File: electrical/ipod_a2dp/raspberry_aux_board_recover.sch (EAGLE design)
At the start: 23 parts, among them IC1 74LS244N

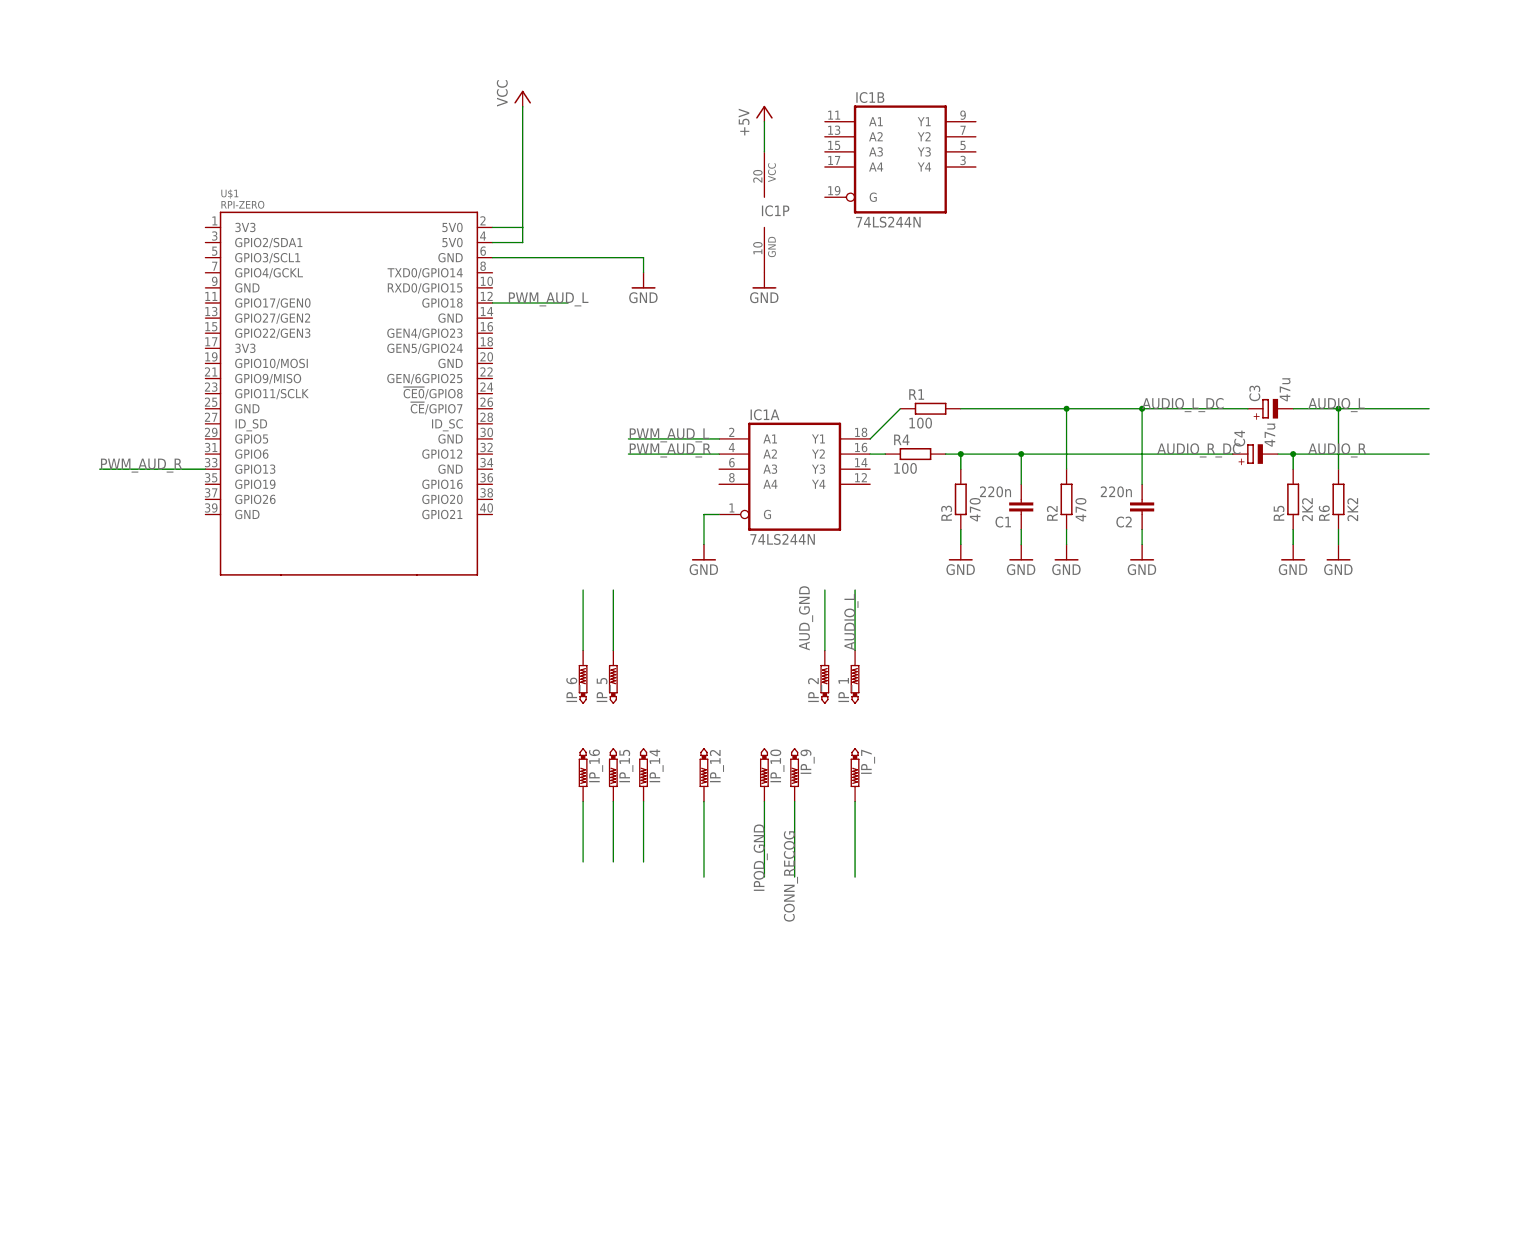
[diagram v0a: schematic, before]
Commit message: more changes. proto tested. working for audio.
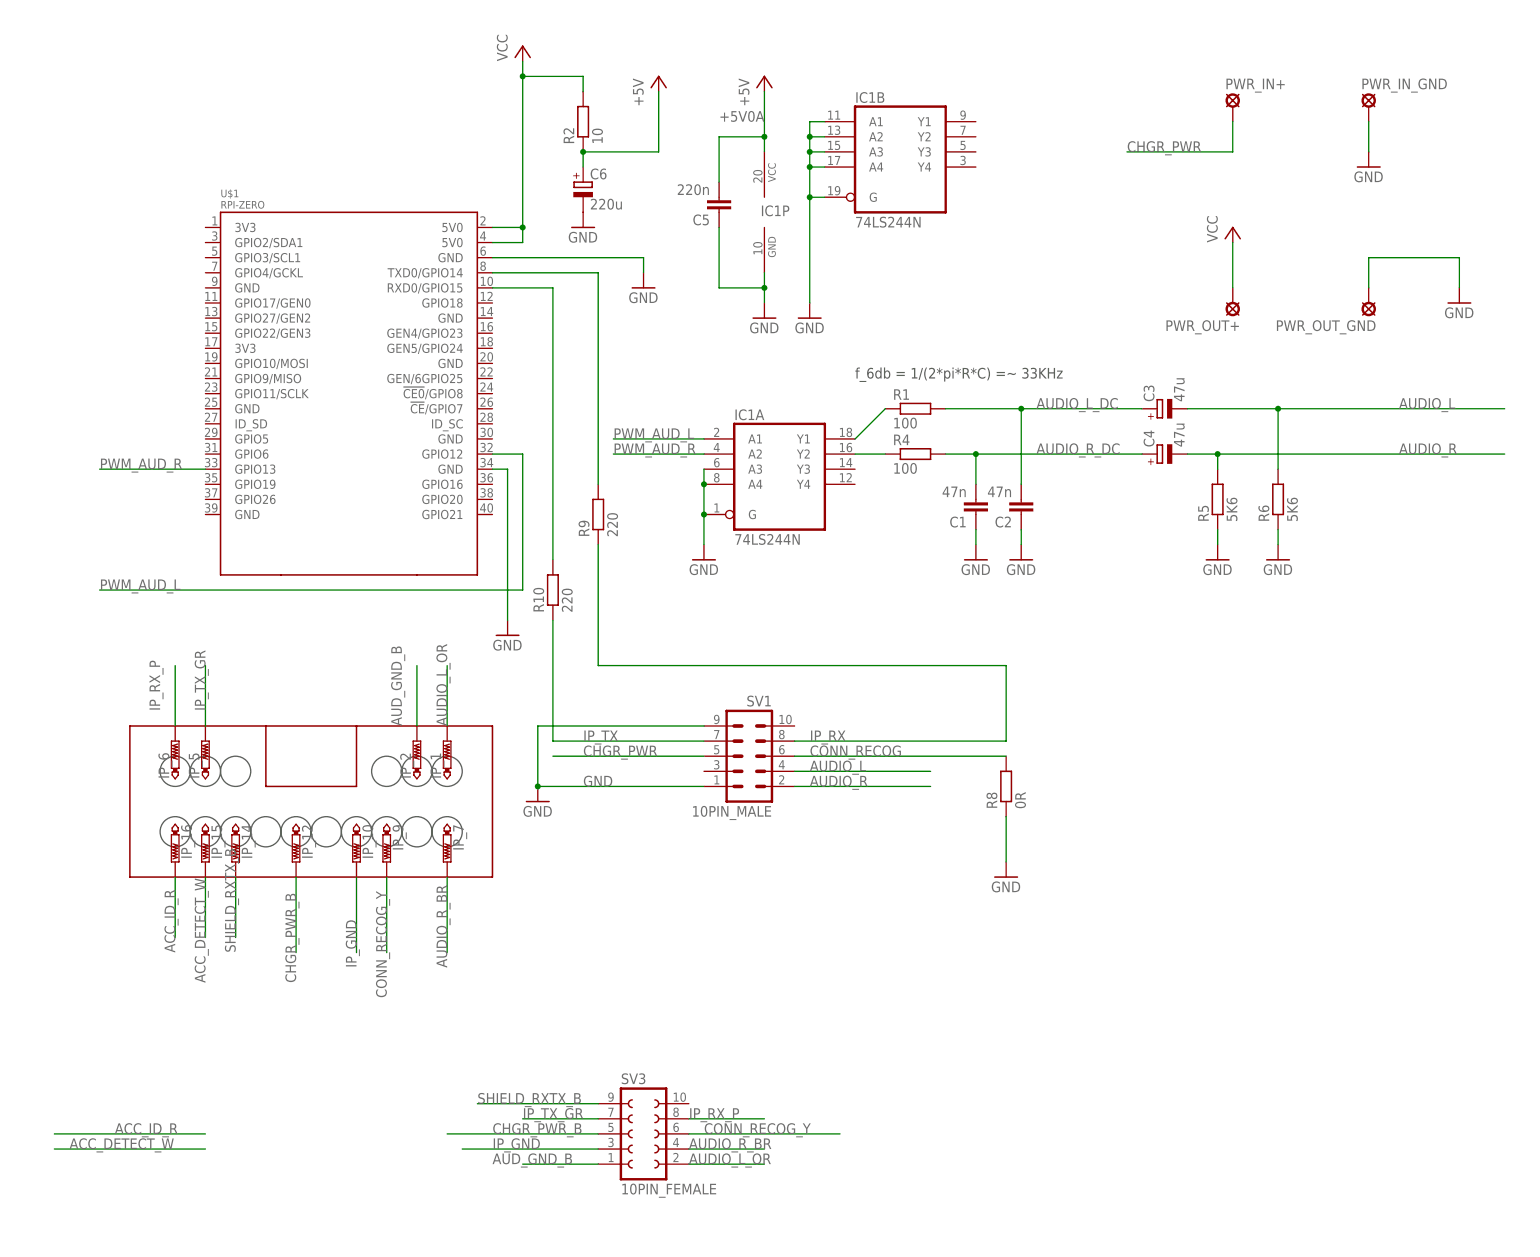
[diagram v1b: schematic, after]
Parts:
- removed R3: 470, rcl:R-EU_0207/10
- added C5: 220n, rcl:C-EU025_050-035X075
- added C6: 220u, rcl:CPOL-EUE2.5-5
- added PWR_IN+, PWR_IN_GND, PWR_OUT+, PWR_OUT_GND: SE13, solpad:SE13
- added R10, R9: 220, rcl:R-EU_0207/10
- added R8: 0R, rcl:R-EU_0207/10
- added SV1: 10PIN_MALE, con-lstb:MA05-2
- added SV3: 10PIN_FEMALE, con-lsta:FE05-2
- C1, C2: value 220n -> 47n
- R2: value 470 -> 10
- R5, R6: value 2K2 -> 5K6
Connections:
- net N$2 renamed ACC_ID_R
- net N$4 renamed ACC_DETECT_W
- removed net +5V: IC1P.VCC
- removed net AUD_GND: IP_2.TP
- removed net IPOD_GND: IP_10.TP
- removed net N$5: IP_5.TP
- removed net N$6: IP_6.TP
- removed net N$7: IP_14.TP
- removed net N$8: IP_12.TP
- new net +5V0A: C5.2, C6.+, IC1P.VCC, R2.1
- new net AUDIO_L_OR: IP_1.TP, SV3.2
- new net AUDIO_R_BR: IP_7.TP, SV3.4
- new net AUD_GND_B: IP_2.TP, SV3.1
- new net CHGR_PWR: PWR_IN+.MP, SV1.5
- new net CHGR_PWR_B: IP_12.TP, SV3.5
- new net CONN_RECOG_Y: IP_9.TP, SV3.6
- new net IP_GND: IP_10.TP, SV3.3
- new net IP_RX: R9.1, SV1.8
- new net IP_RX_P: IP_6.TP, SV3.8
- new net IP_TX: R10.1, SV1.7
- new net IP_TX_GR: IP_5.TP, SV3.7
- new net N$2: R9.2, U$1.TXD0/GPIO14
- new net N$4: R10.2, U$1.RXD0/GPIO15
- new net SHIELD_RXTX_B: IP_14.TP, SV3.9
- net AUDIO_L: now also SV1.4; no longer IP_1.TP
- net AUDIO_L_DC: no longer R2.2
- net AUDIO_R: now also SV1.2; no longer IP_7.TP
- net AUDIO_R_DC: no longer R3.2
- net CONN_RECOG: now also R8.2, SV1.6; no longer IP_9.TP
- net GND: now also C5.1, C6.-, IC1A.A3, IC1A.A4, IC1B.A1, IC1B.A2, IC1B.A3, IC1B.A4, IC1B.G, PWR_IN_GND.MP, PWR_OUT_GND.MP, R8.1, SV1.1, SV1.9, U$1.GND@7; no longer R2.1, R3.1
- net PWM_AUD_L: now also U$1.GPIO12; no longer U$1.GPIO18
- net VCC: now also PWR_OUT+.MP, R2.2
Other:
- note added: "f_6db = 1/(2*pi*R*C) =~ 33KHz"
- moved on the sheet: C1, C2, C3, C4, IC1A, IP_1, IP_10, IP_12, IP_14, IP_15, IP_16, IP_2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

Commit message: updated board
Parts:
- added SV4: 10PIN_MALE, con-lstb:MA05-2
- C1, C2: device rcl:C-EU025_050-035X075 -> rcl:C-EU050-025X075
- C5: device rcl:C-EU025_050-035X075 -> rcl:C-EU050-050X075
- C6: device rcl:CPOL-EUE2.5-5 -> rcl:CPOL-EUE5-13
- R1, R2, R4, R5: device rcl:R-EU_0207/10 -> rcl:R-EU_0204/2V
- R10: device rcl:R-EU_0207/10 -> rcl:R-EU_0207/15
- R9: device rcl:R-EU_0207/10 -> rcl:R-EU_0204/7
- SV1: value 10PIN_MALE -> (none); device con-lstb:MA05-2 -> con-lstb:MA06-1
- renumbered SV3 to SV2
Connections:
- net N$1 renamed PWM_AUDIO_R_OUT
- net N$4 renamed RPI_RX
- removed net N$2: R9.2, U$1.TXD0/GPIO14
- removed net N$3: IC1A.Y2, R4.1
- new net B_GND: SV1.1
- new net OR_TXD: SV1.4
- new net PWM_AUDIO_L_OUT: IC1A.Y3, R4.1
- new net RPI_TX: R9.2, U$1.GPIO4/GCKL, U$1.TXD0/GPIO14
- new net Y_RXD: SV1.5
- net AUDIO_L: now also C4.-, R5.2, SV4.3; no longer C3.-, R6.2, SV1.4
- net AUDIO_L_DC: now also C1.2, C4.+, R4.2; no longer C2.2, C3.+, R1.2
- net AUDIO_L_OR: now also SV2.1; no longer SV2.2
- net AUDIO_R: now also C3.-, R6.2, SV4.1; no longer C4.-, R5.2, SV1.2
- net AUDIO_R_BR: now also SV2.3; no longer SV2.4
- net AUDIO_R_DC: now also C2.2, C3.+, R1.2; no longer C1.2, C4.+, R4.2
- net AUD_GND_B: now also SV2.2; no longer SV2.1
- net CHGR_PWR: now also SV4.6; no longer SV1.5
- net CHGR_PWR_B: now also SV2.6; no longer SV2.5
- net CONN_RECOG: now also SV4.5; no longer SV1.6
- net CONN_RECOG_Y: now also SV2.5; no longer SV2.6
- net GND: now also IC1A.A2, SV4.10, SV4.2; no longer IC1A.A3, SV1.1, SV1.9
- net IP_GND: now also SV2.4; no longer SV2.3
- net IP_RX: now also SV4.7; no longer SV1.8
- net IP_RX_P: now also SV2.7; no longer SV2.8
- net IP_TX: now also SV4.8; no longer SV1.7
- net IP_TX_GR: now also SV2.8; no longer SV2.7
- net PWM_AUD_L: now also IC1A.A3, U$1.GPIO13, U$1.GPIO16; no longer IC1A.A1, U$1.GPIO12
- net PWM_AUD_R: now also IC1A.A1, U$1.GPIO12; no longer IC1A.A2, U$1.GPIO13
- net SHIELD_RXTX_B: now also SV2.10; no longer SV2.9

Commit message: update board and schematic. update daemon for ipod emul
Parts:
- added H1, H2, H3, H4: MOUNT-HOLE2.8, holes:MOUNT-HOLE2.8
- C6: device rcl:CPOL-EUE5-13 -> rcl:CPOL-EUE5-10.5
- IP_1, IP_10, IP_12, IP_14, IP_15, IP_16, IP_2, IP_5, IP_6, IP_7, IP_9: value PTR1PAD1-17 -> X; device testpad:PTR1PAD1-17 -> wirepad:2,15/1,0
- R6: device rcl:R-EU_0207/10 -> rcl:R-EU_0204/7
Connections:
- removed net PWM_AUDIO_L_OUT: IC1A.Y3, R4.1
- removed net PWM_AUDIO_R_OUT: IC1A.Y1, R1.1
- new net N$1: IC1A.Y4, R4.1
- new net N$2: IC1A.Y2, R1.1
- net ACC_DETECT_W: now also IP_15.P; no longer IP_15.TP
- net ACC_ID_R: now also IP_16.P; no longer IP_16.TP
- net AUDIO_L_OR: now also IP_1.P; no longer IP_1.TP
- net AUDIO_R_BR: now also IP_7.P; no longer IP_7.TP
- net AUD_GND_B: now also IP_2.P; no longer IP_2.TP
- net CHGR_PWR_B: now also IP_12.P; no longer IP_12.TP
- net CONN_RECOG_Y: now also IP_9.P; no longer IP_9.TP
- net GND: now also IC1A.A1, IC1A.A3, SV4.9; no longer IC1A.A2, IC1A.A4, PWR_OUT_GND.MP
- net IP_GND: now also IP_10.P; no longer IP_10.TP
- net IP_RX_P: now also IP_6.P; no longer IP_6.TP
- net IP_TX_GR: now also IP_5.P; no longer IP_5.TP
- net PWM_AUD_L: now also IC1A.A4; no longer IC1A.A3
- net PWM_AUD_R: now also IC1A.A2; no longer IC1A.A1
- net SHIELD_RXTX_B: now also IP_14.P; no longer IP_14.TP

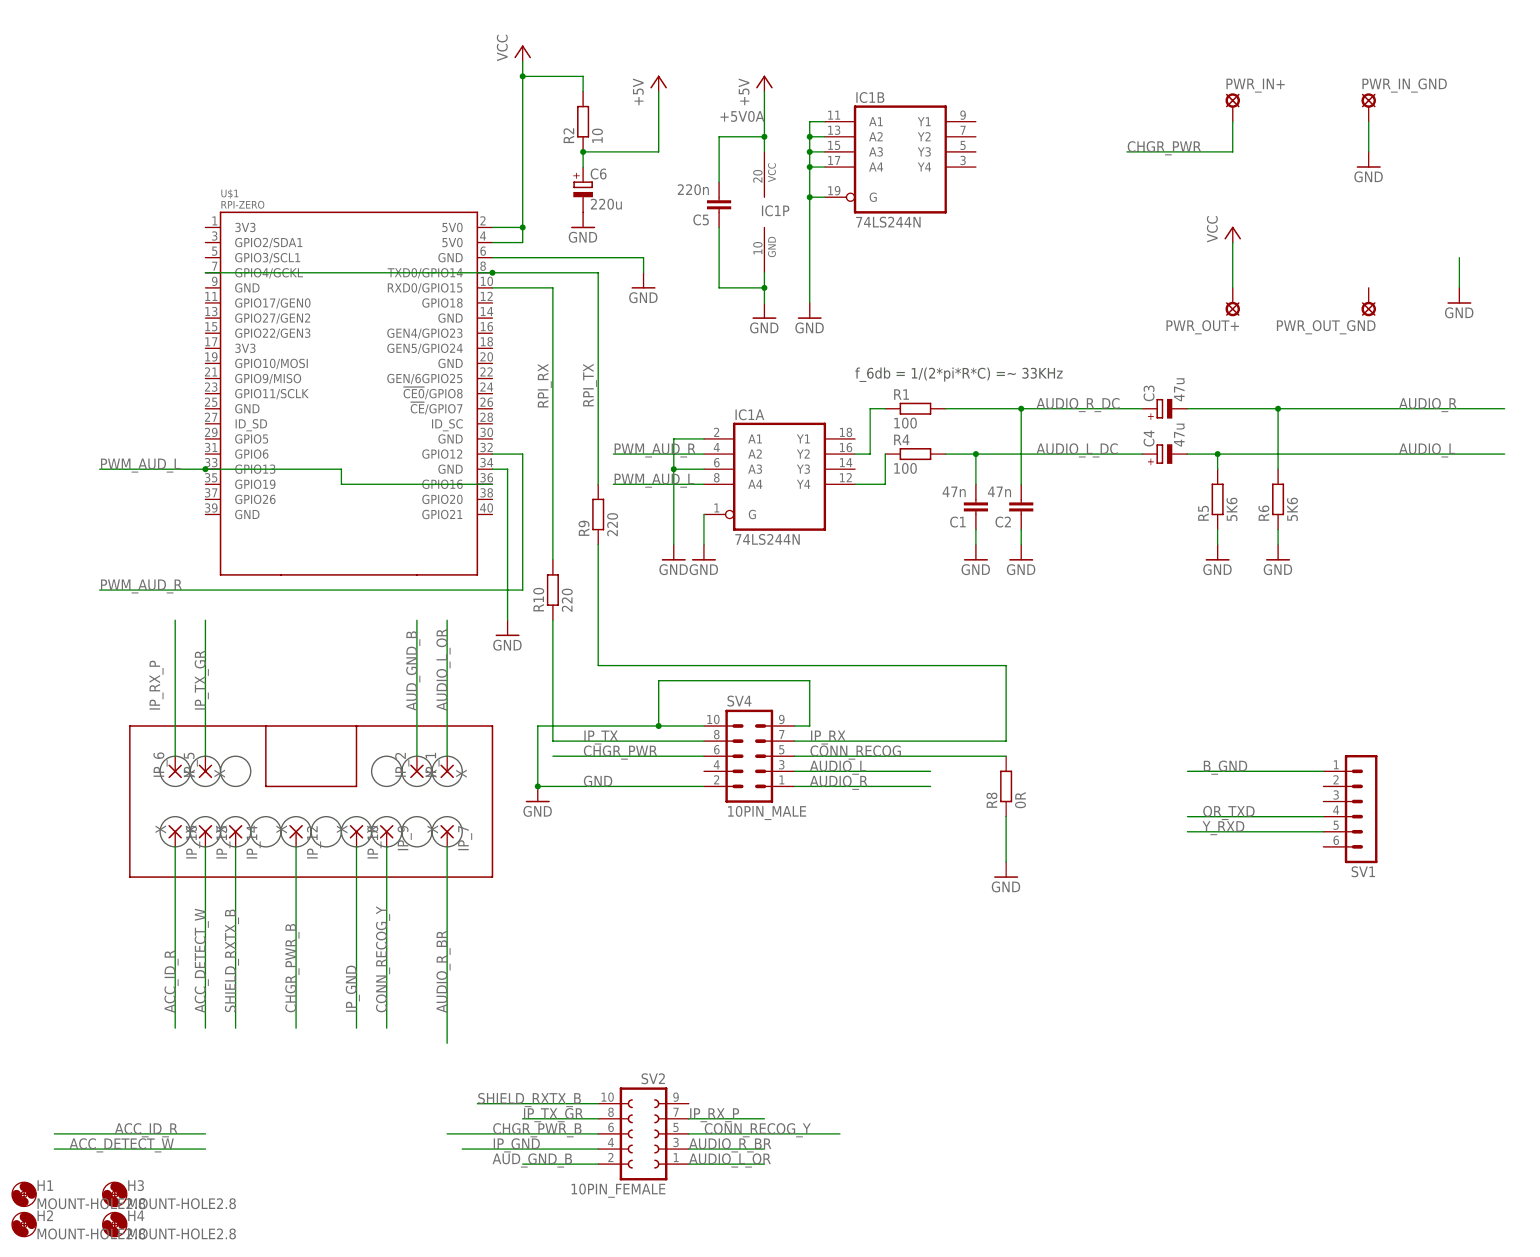
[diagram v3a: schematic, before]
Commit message: updated schematic and board. sent to production
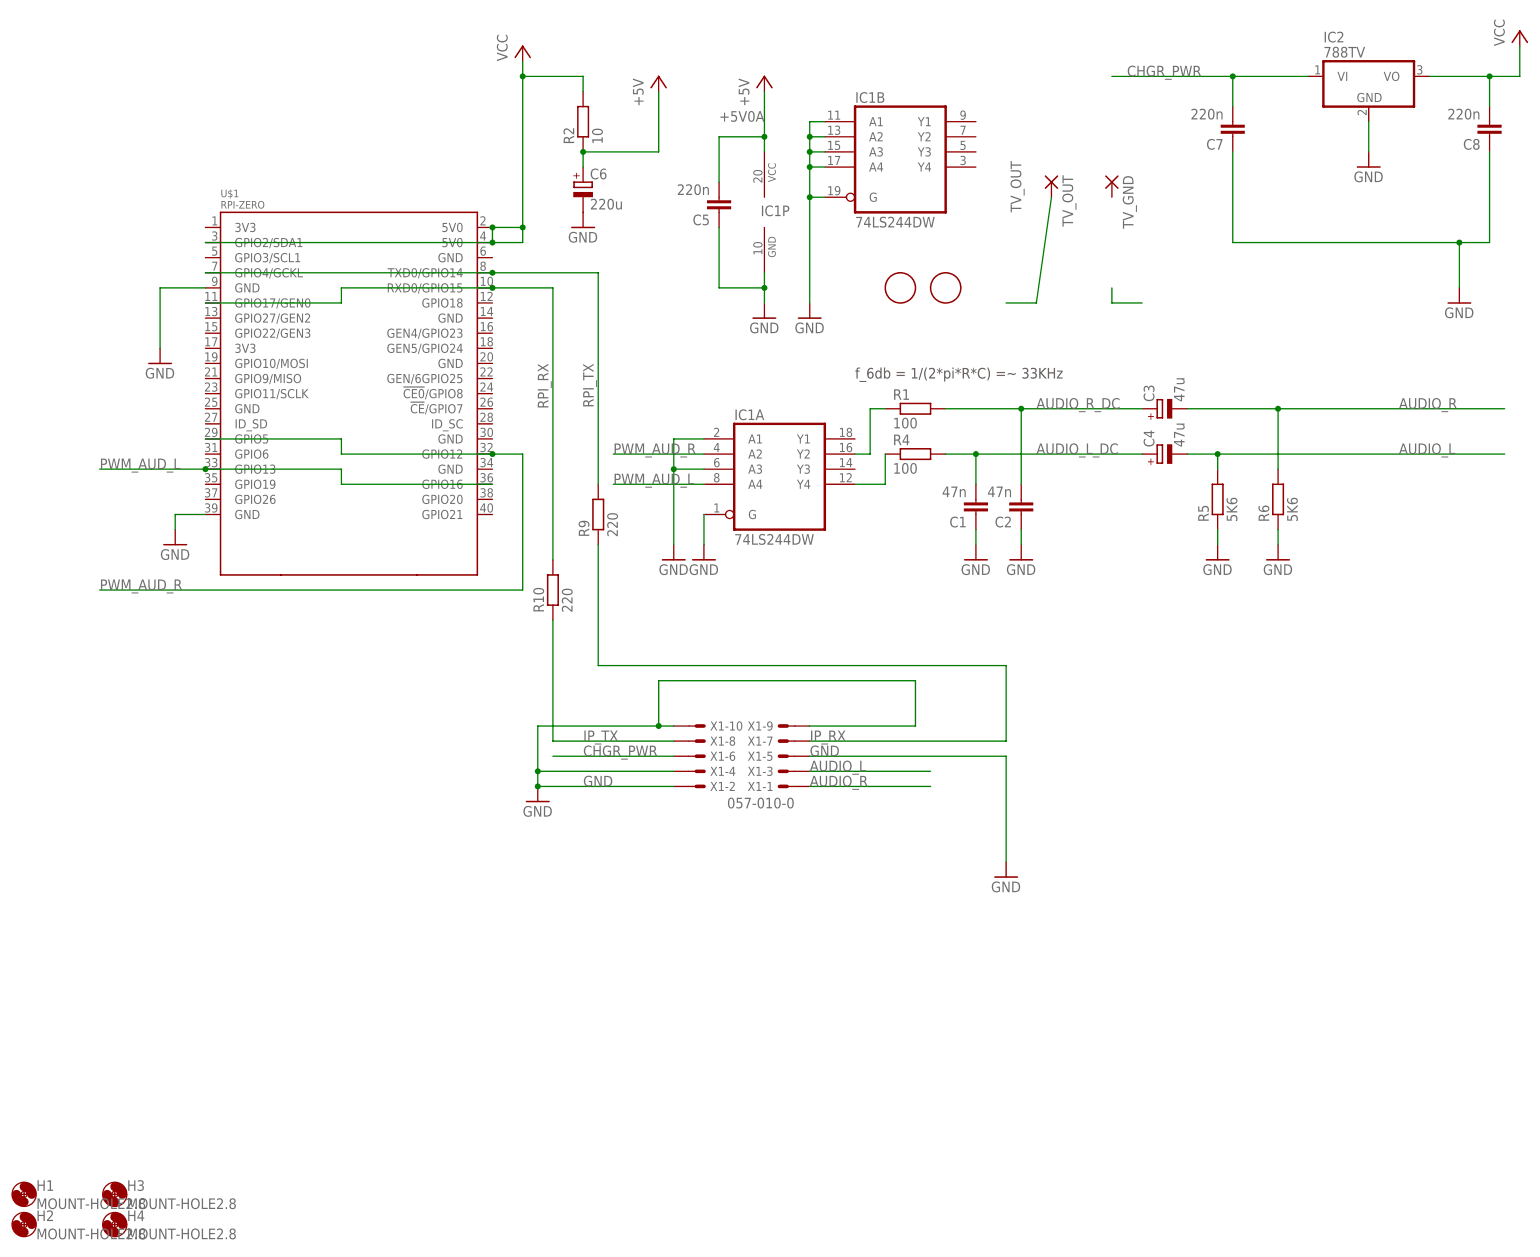
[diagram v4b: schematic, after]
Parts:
- removed IP_1, IP_10, IP_12, IP_14, IP_15, IP_16, IP_2, IP_5, IP_6, IP_7, IP_9: X, wirepad:2,15/1,0
- removed PWR_IN+, PWR_IN_GND, PWR_OUT+, PWR_OUT_GND: SE13, solpad:SE13
- removed R8: 0R, rcl:R-EU_0207/10
- removed SV1: (no value), con-lstb:MA06-1
- removed SV2: 10PIN_FEMALE, con-lsta:FE05-2
- removed SV4: 10PIN_MALE, con-lstb:MA05-2
- added C7, C8: 220n, rcl:C-EU050-050X075
- added IC2: 788TV, linear:788TV
- added TV_GND, TV_OUT: (no value), wirepad:2,15/1,0
- added U$2, U$3: FIDUCIAL, adafruit:FIDUCIAL
- added X1: 057-010-0, con-panduit:057-010-0
- IC1: value 74LS244N -> 74LS244DW; device 74xx-us:74LS244N -> 74xx-us:74LS244DW
- R1: device rcl:R-EU_0204/2V -> rcl:R-EU_0207/10
- R2, R4, R5: device rcl:R-EU_0204/2V -> rcl:R-EU_0204/7
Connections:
- removed net ACC_DETECT_W: IP_15.P
- removed net ACC_ID_R: IP_16.P
- removed net AUDIO_L_OR: IP_1.P, SV2.1
- removed net AUDIO_R_BR: IP_7.P, SV2.3
- removed net AUD_GND_B: IP_2.P, SV2.2
- removed net B_GND: SV1.1
- removed net CHGR_PWR_B: IP_12.P, SV2.6
- removed net CONN_RECOG: R8.2, SV4.5
- removed net CONN_RECOG_Y: IP_9.P, SV2.5
- removed net IP_GND: IP_10.P, SV2.4
- removed net IP_RX_P: IP_6.P, SV2.7
- removed net IP_TX_GR: IP_5.P, SV2.8
- removed net OR_TXD: SV1.4
- removed net SHIELD_RXTX_B: IP_14.P, SV2.10
- removed net Y_RXD: SV1.5
- new net TV_OUT: TV_OUT.P
- net AUDIO_L: now also X1-3.S; no longer SV4.3
- net AUDIO_R: now also X1-1.S; no longer SV4.1
- net CHGR_PWR: now also C7.2, IC2.VI, X1-6.S; no longer PWR_IN+.MP, SV4.6
- net GND: now also C7.1, C8.1, IC2.GND, U$1.GND@1, U$1.GND@3, X1-10.S, X1-2.S, X1-4.S, X1-5.S, X1-9.S; no longer PWR_IN_GND.MP, R8.1, SV4.10, SV4.2, SV4.9, U$1.GND@7, U$1.GND@8
- net IP_RX: now also X1-7.S; no longer SV4.7
- net IP_TX: now also X1-8.S; no longer SV4.8
- net PWM_AUD_R: now also U$1.GPIO5
- net RPI_RX: now also U$1.GPIO17/GEN0
- net VCC: now also C8.2, IC2.VO, U$1.GPIO2/SDA1; no longer PWR_OUT+.MP
